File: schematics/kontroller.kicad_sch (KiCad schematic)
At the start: 10 parts

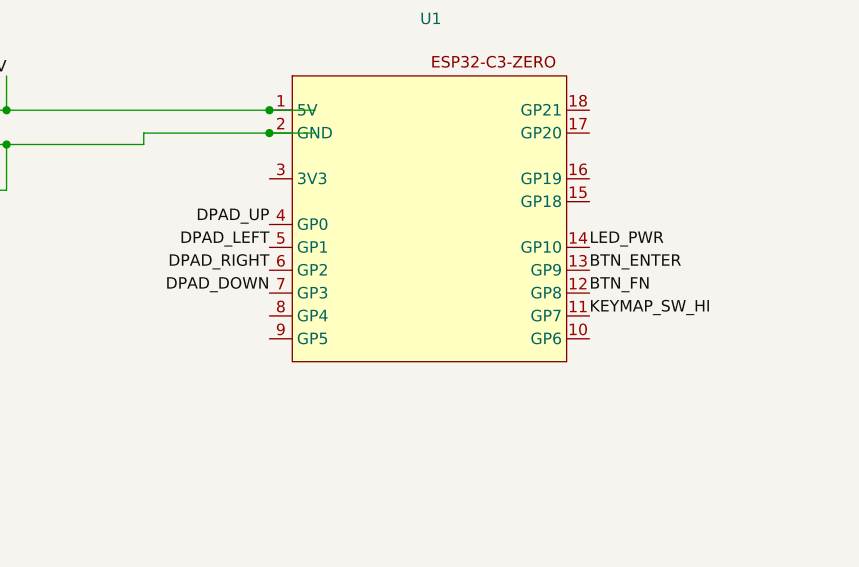
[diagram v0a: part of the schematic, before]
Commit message: feat: add symbols library, update diagram to match kicad
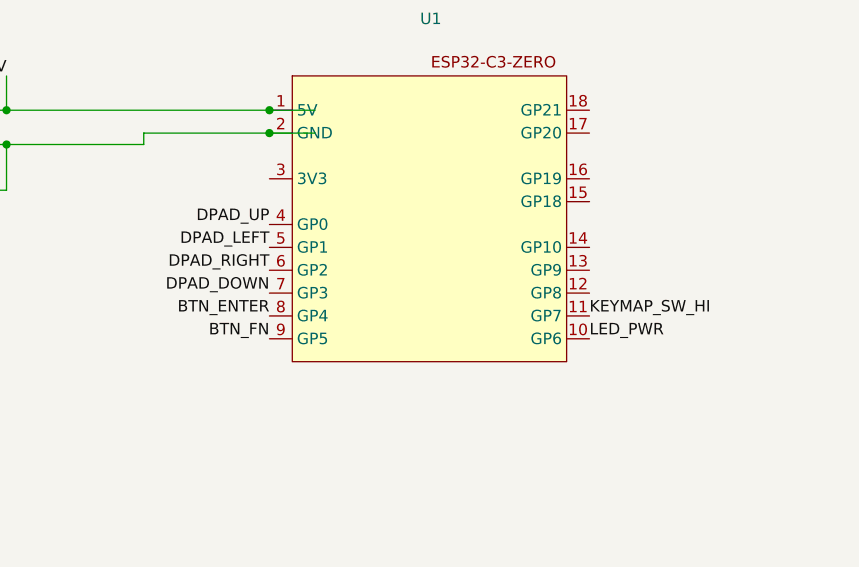
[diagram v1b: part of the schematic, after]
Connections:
- net BTN_ENTER: now also U1.8 (GP4); no longer U1.13 (GP9)
- net BTN_FN: now also U1.9 (GP5); no longer U1.12 (GP8)
- net LED_PWR: now also U1.10 (GP6); no longer U1.14 (GP10)
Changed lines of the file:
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@@
 	)
 	(label "BTN_FN"
-		(at 163.83 107.95 0)
+		(at 128.27 113.03 180)
 		(fields_autoplaced yes)
 		(effects
@@
 				(size 1.27 1.27)
 			)
-			(justify left bottom)
+			(justify right bottom)
 		)
 	)
 	(label "LED_PWR"
-		(at 163.83 102.87 0)
+		(at 163.83 113.03 0)
 		(fields_autoplaced yes)
 		(effects
@@
 	)
 	(label "BTN_ENTER"
-		(at 163.83 105.41 0)
+		(at 128.27 110.49 180)
 		(fields_autoplaced yes)
 		(effects
@@
 				(size 1.27 1.27)
 			)
-			(justify left bottom)
+			(justify right bottom)
 		)
 	)
